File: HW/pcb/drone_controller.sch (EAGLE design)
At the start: 20 parts, among them J1 SM08B-SRSS-TB, U1 ICM-20600, U2 VXO7805-500, U3 CD40109BE

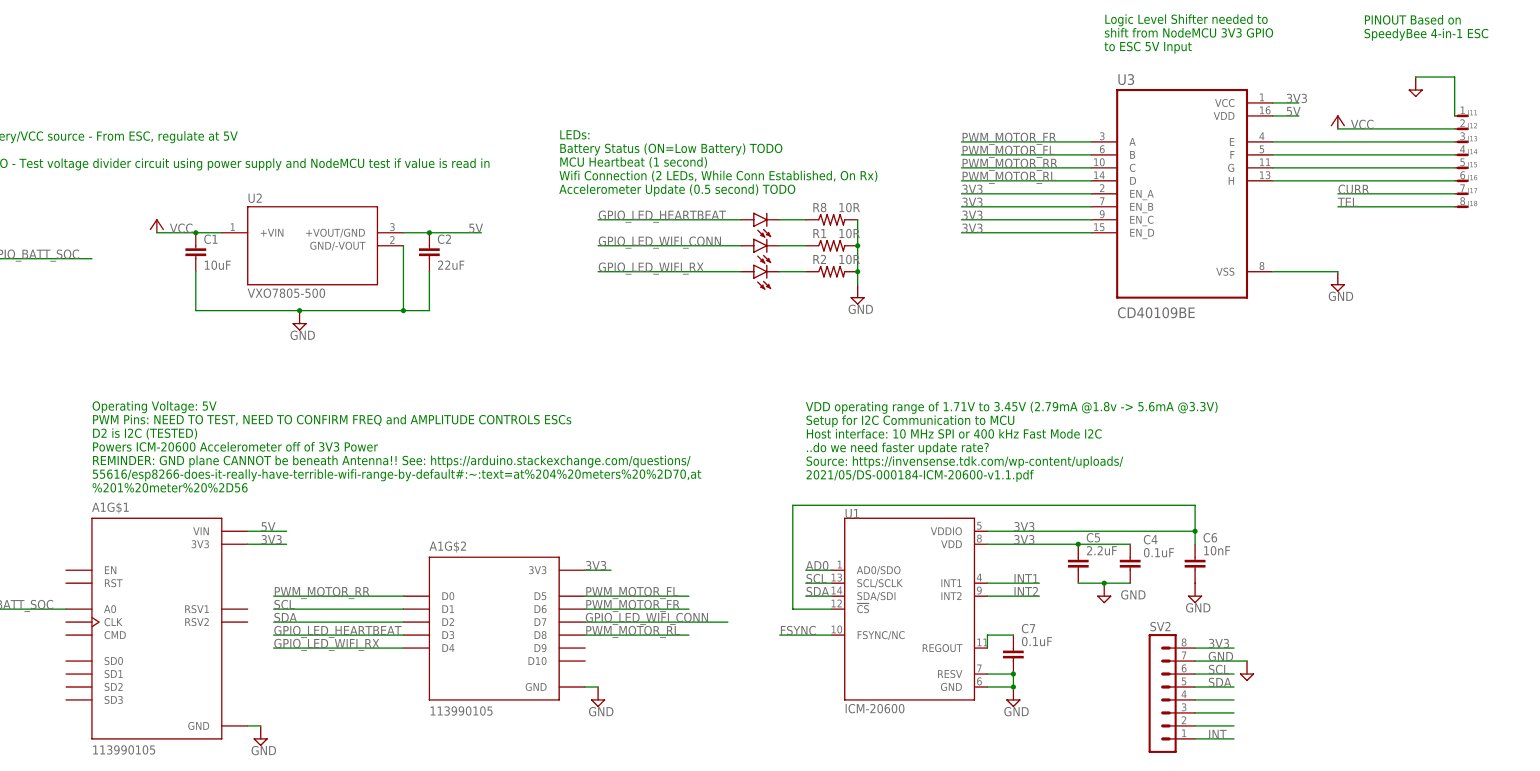
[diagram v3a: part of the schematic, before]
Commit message: removed 3.3V to 5V level shifter. not needed for this ESC (SpeedyBee 4-in-1 ESC). Placed components on board in more organized layout. Routed Board. All Airwires routed. Added Ground planes with stiching vias
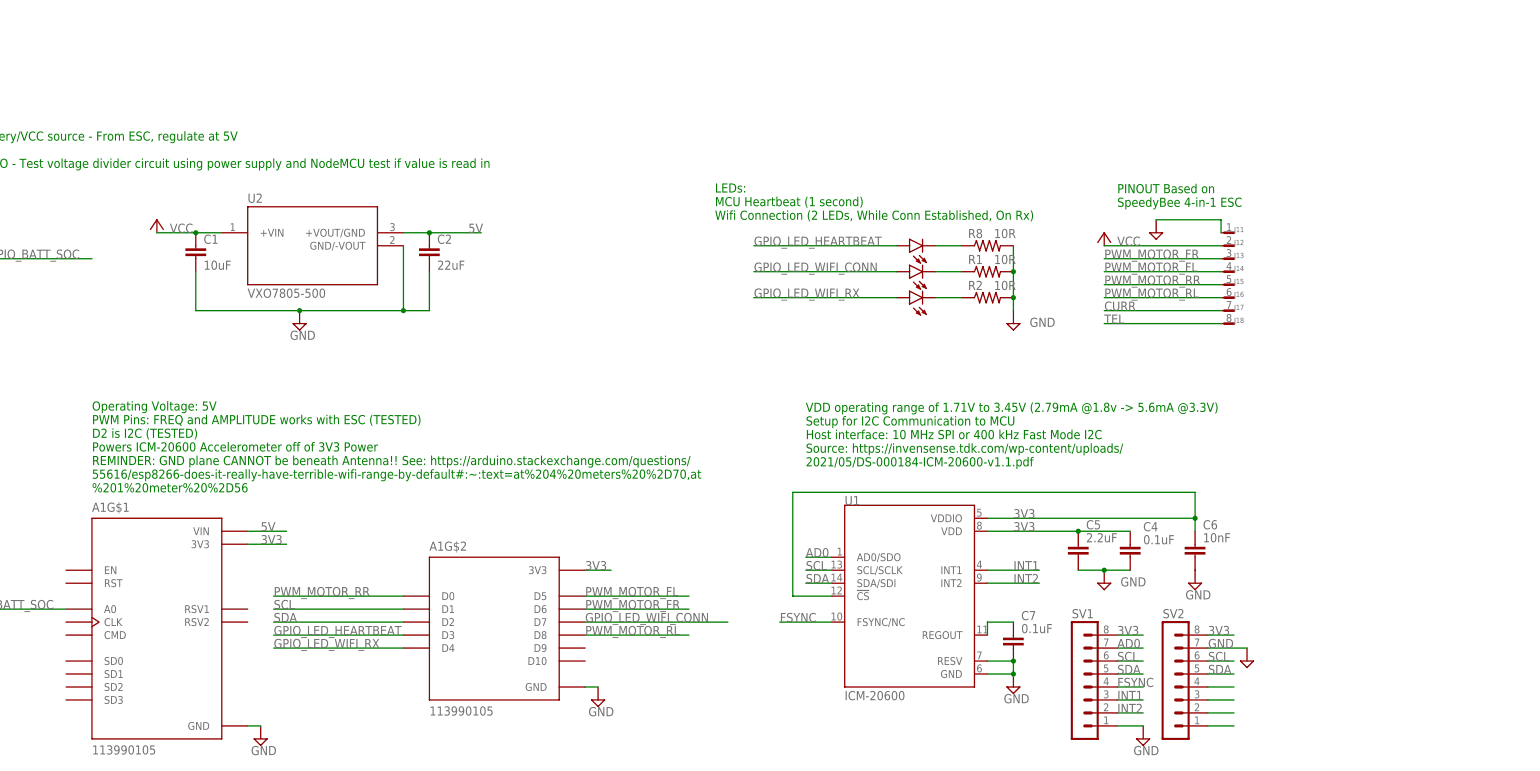
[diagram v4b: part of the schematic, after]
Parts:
- removed U3: CD40109BE, CD40109BE:CD40109BE
- added SV1: (no value), con-lstb:MA08-1
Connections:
- removed net N$11: J16.P, U3.H
- removed net N$2: J13.P, U3.E
- removed net N$3: J14.P, U3.F
- removed net N$4: J15.P, U3.G
- net 3V3: now also SV1.8; no longer U3.EN_A, U3.EN_B, U3.EN_C, U3.EN_D, U3.VCC
- net 5V: no longer U3.VDD
- net AD0: now also SV1.7
- net FSYNC: now also SV1.4
- net GND: now also SV1.1; no longer U3.VSS
- net INT1: now also SV1.3
- net INT2: now also SV1.2
- net PWM_MOTOR_FL: now also J14.P; no longer U3.B
- net PWM_MOTOR_FR: now also J13.P; no longer U3.A
- net PWM_MOTOR_RL: now also J16.P; no longer U3.D
- net PWM_MOTOR_RR: now also J15.P; no longer U3.C
- net SCL: now also SV1.6
- net SDA: now also SV1.5
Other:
- note added: "LEDs: MCU Heartbeat (1 second) Wifi Connection (2 LEDs, While Conn Established, On Rx)"
- note added: "Operating Voltage: 5V PWM Pins: FREQ and AMPLITUDE works with ESC (TESTED) D2 is I2C (TESTED) Powers ICM-20600 Accelerometer off of 3V3 Power REMINDER: GND plane CANNOT be beneath Antenna!! See: https://arduino.stackexchange.com/questions/ 55616/esp8266-does-it-really-have-terrible-wifi-range-by-default#:~:text=at%204%20meters%20%2D70,at %201%20meter%20%2D56"
- note added: "VDD operating range of 1.71V to 3.45V (2.79mA @1.8v -> 5.6mA @3.3V) Setup for I2C Communication to MCU Host interface: 10 MHz SPI or 400 kHz Fast Mode I2C Source: https://invensense.tdk.com/wp-content/uploads/ 2021/05/DS-000184-ICM-20600-v1.1.pdf"
- note removed: "LEDs: Battery Status (ON=Low Battery) TODO MCU Heartbeat (1 second) Wifi Connection (2 LEDs, While Conn Established, On Rx) Accelerometer Update (0.5 second) TODO"
- note removed: "Logic Level Shifter needed to shift from NodeMCU 3V3 GPIO to ESC 5V Input"
- note removed: "Operating Voltage: 5V PWM Pins: NEED TO TEST, NEED TO CONFIRM FREQ and AMPLITUDE CONTROLS ESCs D2 is I2C (TESTED) Powers ICM-20600 Accelerometer off of 3V3 Power REMINDER: GND plane CANNOT be beneath Antenna!! See: https://arduino.stackexchange.com/questions/ 55616/esp8266-does-it-really-have-terrible-wifi-range-by-default#:~:text=at%204%20meters%20%2D70,at %201%20meter%20%2D56"
- note removed: "VDD operating range of 1.71V to 3.45V (2.79mA @1.8v -> 5.6mA @3.3V) Setup for I2C Communication to MCU Host interface: 10 MHz SPI or 400 kHz Fast Mode I2C ..do we need faster update rate? Source: https://invensense.tdk.com/wp-content/uploads/ 2021/05/DS-000184-ICM-20600-v1.1.pdf"
- moved on the sheet: C4, C5, C6, C7, J11, J12, J13, J14, J15, J16, J17, J18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

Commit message: ordered V1.1 of drone PCB
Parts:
- removed A1: 113990105, 113990105:113990105
- added C10: 0.1uF, capacitor-wima:C2,5-3
- added C11: 1uF, capacitor-wima:C2,5-3
- added C3, C8: 0.1uF, rcl:C-USC0603
- added C9: 10uF, capacitor-wima:C2,5-3
- added J2: 629105136821, Eagle_WR-USB (rev22c):629105136821
- added JP1: (no value), pinhead:PINHD-1X5
- added R4, R5: 0R, rcl:R-US_0204/7
- added R9: 10K, rcl:R-US_0204/7
- added SJ1, SJ2, SJ3: (no value), jumper:SJ
- added SV3: (no value), con-lstb:MA04-1
- added U3: M24C02-WMN6TP, M24C02-WMN6TP:M24C02-WMN6TP
- added U4: ESP32-C3-MINI-1-N4, ESP32-C3-MINI-1-N4:ESP32-C3-MINI-1-N4
- U2: value VXO7805-500 -> PXO7803-500-S; device VXO7805-500:VXO7805-500 -> PXO7803-500-S:PXO7803-500-S
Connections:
- removed net 5V: A1G$1.VIN, C2.1, U2.+VOUT/GND
- removed net INT: SV2.1
- removed net N$17: SV2.4
- removed net N$18: SV2.3
- removed net N$19: SV2.2
- new net N$2: JP1.5
- new net N$3: C11.1, R9.1, U4.EN
- new net N$6: SJ1.2, U3.E0
- new net N$7: SJ2.2, U3.E1
- new net N$8: SJ3.2, U3.E2
- new net RX: SV3.3, U4.RXD0
- new net TX: SV3.2, U4.TXD0
- new net USB_D_N: C3.1, J2.D-, R4.2
- new net USB_D_P: C8.1, J2.D+, R5.2
- new net USB_RD_N: R4.1, U4.IO18
- new net USB_RD_P: R5.1, U4.IO19
- new net USB_VCC: J2.VBUS
- net 3V3: now also C10.1, C2.1, C9.1, R9.2, SJ1.1, SJ2.1, SJ3.1, SV3.1, U2.VOUT/GND, U3.VCC, U4.3V3; no longer A1G$1.3V3, A1G$2.3V3
- net GND: now also C10.2, C11.2, C3.2, C8.2, C9.2, J2.GND, JP1.1, SV3.4, U3.VSS, U3.~WC, U4.GND; no longer A1G$1.GND, A1G$2.GND
- net GPIO_BATT_SOC: now also U4.IO0; no longer A1G$1.A0
- net GPIO_LED_HEARTBEAT: now also U4.IO6; no longer A1G$2.D3
- net GPIO_LED_WIFI_CONN: now also U4.IO9; no longer A1G$2.D7
- net GPIO_LED_WIFI_RX: now also U4.IO5; no longer A1G$2.D4
- net PWM_MOTOR_FL: now also JP1.3, U4.IO1; no longer A1G$2.D5
- net PWM_MOTOR_FR: now also JP1.2, U4.IO2; no longer A1G$2.D6
- net PWM_MOTOR_RL: now also U4.IO3; no longer A1G$2.D8
- net PWM_MOTOR_RR: now also JP1.4, U4.IO4; no longer A1G$2.D0
- net SCL: now also U3.SCL, U4.IO8; no longer A1G$2.D1
- net SDA: now also U3.SDA, U4.IO7; no longer A1G$2.D2
- net VCC: now also U2.VIN; no longer U2.+VIN
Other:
- note added: "Battery/VCC source - From ESC, regulate at 3.3V"
- note added: "LEDs: MCU Heartbeat Wifi Connection (2 LEDs, While Conn Established, On Rx)"
- note added: "Operating Voltage: 3.3V"
- note removed: "Battery/VCC source - From ESC, regulate at 5V TODO - Test voltage divider circuit using power supply and NodeMCU test if value is read in"
- note removed: "LEDs: MCU Heartbeat (1 second) Wifi Connection (2 LEDs, While Conn Established, On Rx)"
- note removed: "Operating Voltage: 5V PWM Pins: FREQ and AMPLITUDE works with ESC (TESTED) D2 is I2C (TESTED) Powers ICM-20600 Accelerometer off of 3V3 Power REMINDER: GND plane CANNOT be beneath Antenna!! See: https://arduino.stackexchange.com/questions/ 55616/esp8266-does-it-really-have-terrible-wifi-range-by-default#:~:text=at%204%20meters%20%2D70,at %201%20meter%20%2D56"
- moved on the sheet: C1, C2, C4, C5, C6, C7, J11, J12, J13, J14, J15, J16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
